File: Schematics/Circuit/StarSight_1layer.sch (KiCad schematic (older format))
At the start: 40 parts, among them IC1 LM2956-5V, J1 IR1, J10 Line1, J11 Conn_01x02, J12 Conn_01x02, J13 Conn_01x02, J14 ultSound1, J15 Conn_02x02_Counter_Clockwise, J16 ultSound1, J17 Conn_02x02_Counter_Clockwise, J18 ultSound1, J19 Conn_02x02_Counter_Clockwise, J2 Line5, J20 ultSound1, J21 Conn_01x01, J22 Conn_01x01, J23 Conn_01x01, J3 IR1, J4 Line4, J5 IR1, J6 Line3, J7 IR1, J8 Line2, J9 IR1, K1 RELAY, K2 RELAY, P1 CONN_13X2, P2 Power, Q1 Q_NMOS_GDS, Q2 Q_NMOS_GDS

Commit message: Change inductor footprint
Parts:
- L1: footprint Diodes_THT:D_5W_P5.08mm_Vertical_KathodeUp -> Inductors_THT:L_Toroid_Vertical_L16.0mm_W8.0mm_P7.62mm
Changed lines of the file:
@@
 F 0 "L1" V 3100 4500 50  0000 C CNN
 F 1 "33 uH" V 3225 4500 50  0000 C CNN
-F 2 "Diodes_THT:D_5W_P5.08mm_Vertical_KathodeUp" H 3150 4500 50  0001 C CNN
+F 2 "Inductors_THT:L_Toroid_Vertical_L16.0mm_W8.0mm_P7.62mm" H 3150 4500 50  0001 C CNN
 F 3 "" H 3150 4500 50  0001 C CNN
 	1    3150 4500

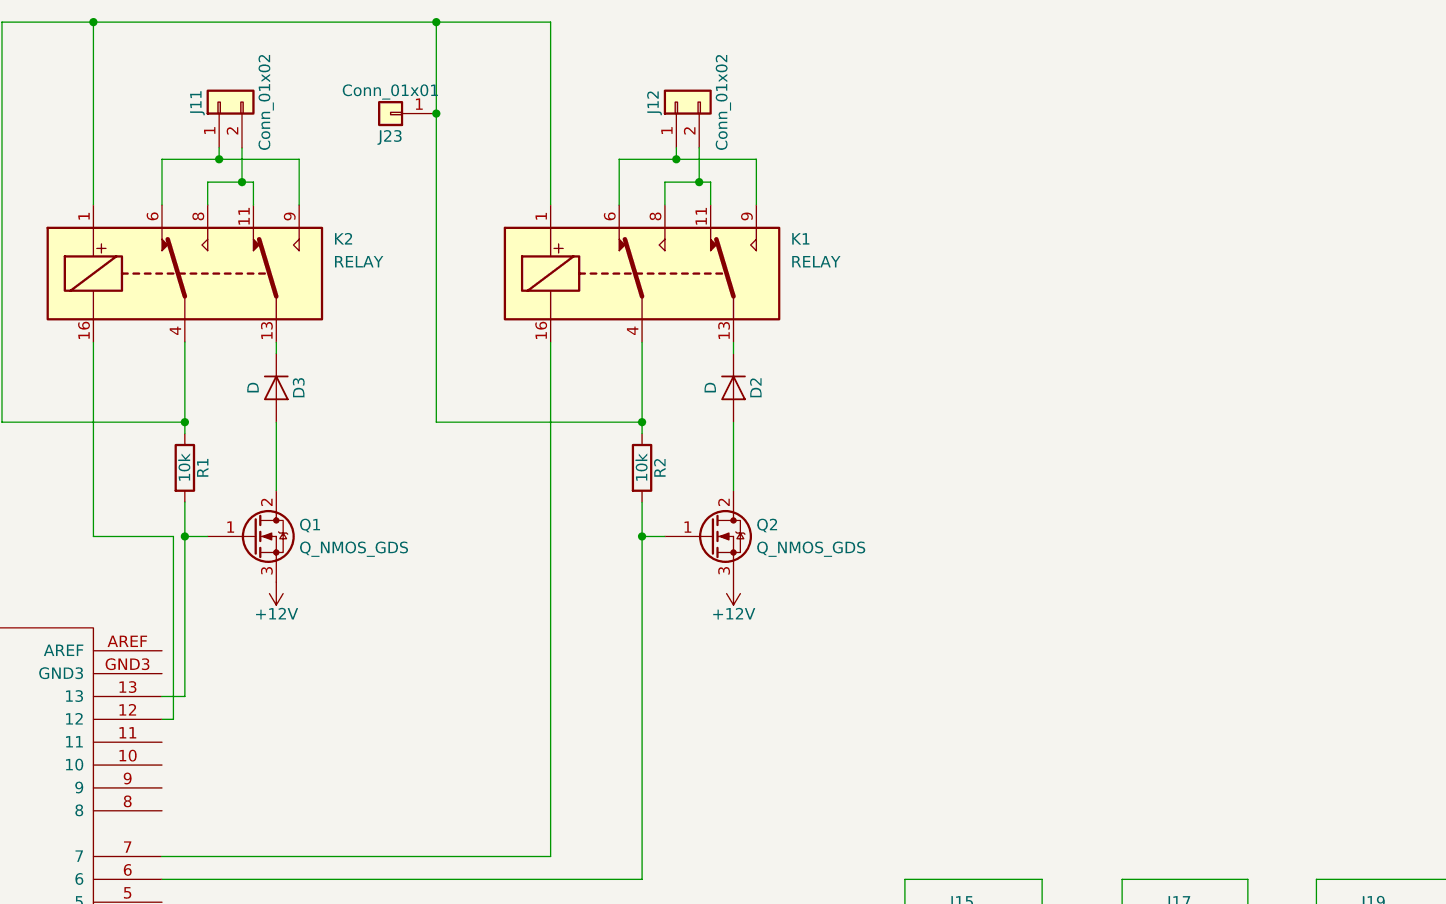
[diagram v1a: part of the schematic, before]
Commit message: Add fan
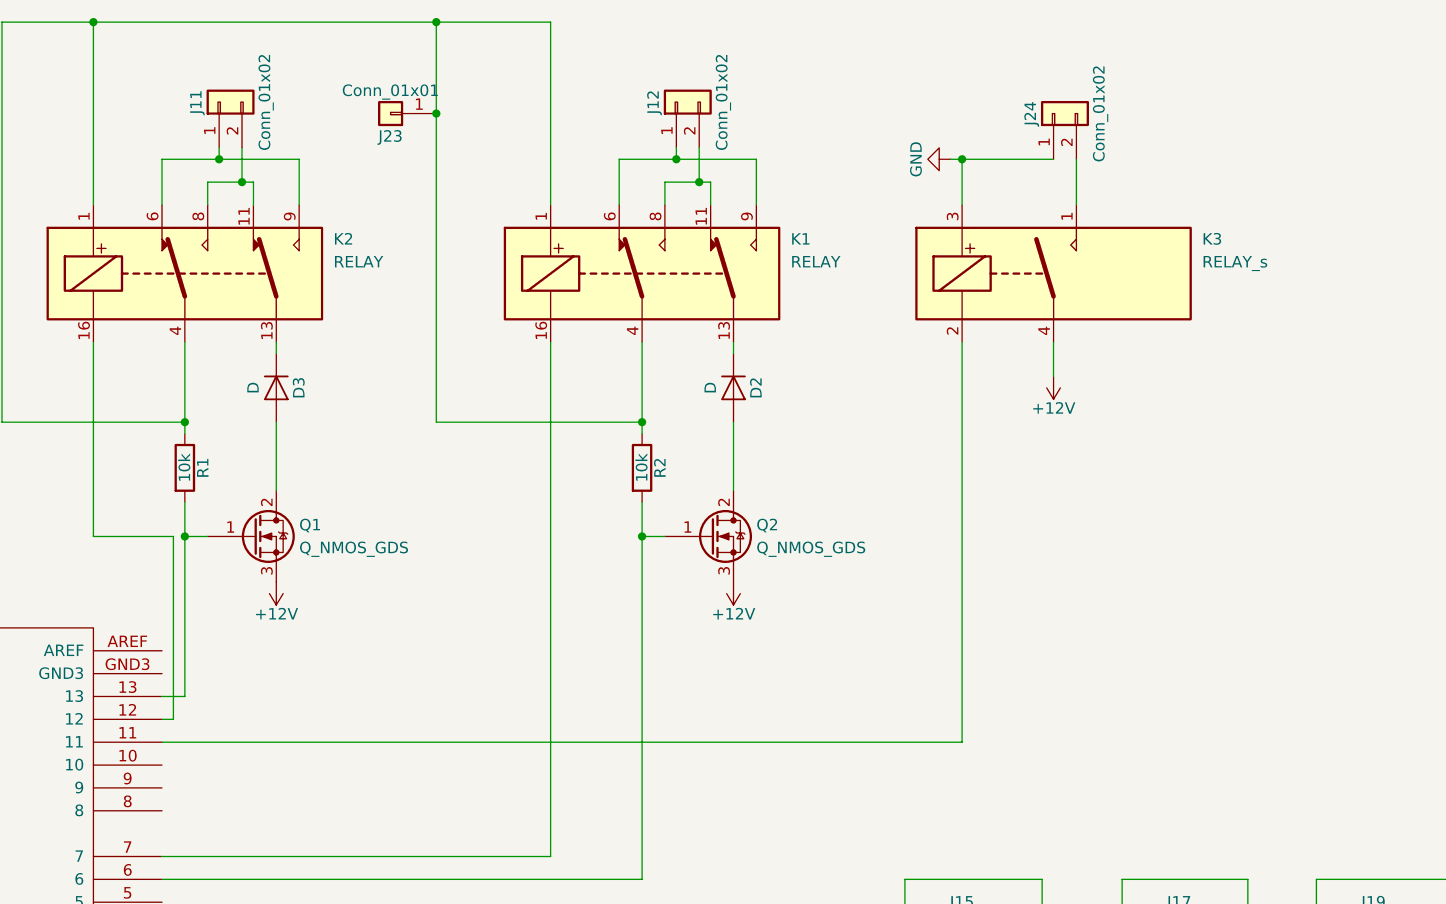
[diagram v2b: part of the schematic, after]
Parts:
- added J24: Conn_01x02, Pin_Headers:Pin_Header_Straight_1x02_Pitch2.54mm, symbol Conn_01x02
- added K3: RELAY_s, starsight:RELAY_s, symbol RELAY_s
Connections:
- net +12V: now also K3.4
- net GND: now also J24.1 (Pin_1), K3.3
- net at SHIELD1.11: now also K3.2
- new net: J24.2 (Pin_2), K3.1
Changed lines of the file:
@@
 	8950 850  11350 850
 Wire Wire Line
-	10850 2600 10850 850
+	10850 850  10850 2600
 Wire Wire Line
 	11750 4600 9650 4600
@@
 	1    0    0    -1
 $EndComp
+$Comp
+L RELAY_s K3
+U 1 1 5A820B81
+P 13350 1950
+F 0 "K3" H 14200 2100 50  0000 L CNN
+F 1 "RELAY_s" H 14200 2000 50  0000 L CNN
+F 2 "starsight:RELAY_s" H 14100 2000 50  0001 C CNN
+F 3 "" H 13350 1950 50  0001 C CNN
+	1    13350 1950
+	1    0    0    -1
+$EndComp
+Wire Wire Line
+	9650 4000 13150 4000
+Wire Wire Line
+	13150 4000 13150 2250
+$Comp
+L GND #PWR017
+U 1 1 5A821524
+P 13100 1450
+F 0 "#PWR017" H 13100 1200 50  0001 C CNN
+F 1 "GND" H 13100 1300 50  0000 C CNN
+F 2 "" H 13100 1450 50  0001 C CNN
+F 3 "" H 13100 1450 50  0001 C CNN
+	1    13100 1450
+	0    1    1    0
+$EndComp
+$Comp
+L Conn_01x02 J24
+U 1 1 5A8216F2
+P 13550 1250
+F 0 "J24" H 13550 1350 50  0000 C CNN
+F 1 "Conn_01x02" H 13550 1050 50  0000 C CNN
+F 2 "Pin_Headers:Pin_Header_Straight_1x02_Pitch2.54mm" H 13550 1250 50  0001 C CNN
+F 3 "" H 13550 1250 50  0001 C CNN
+	1    13550 1250
+	0    -1   -1   0
+$EndComp
+Wire Wire Line
+	13150 1650 13150 1450
+Wire Wire Line
+	13100 1450 13550 1450
+Connection ~ 13150 1450
+Wire Wire Line
+	13650 1650 13650 1450
+$Comp
+L +12V #PWR018
+U 1 1 5A821FE2
+P 13550 2400
+F 0 "#PWR018" H 13550 2250 50  0001 C CNN
+F 1 "+12V" H 13550 2540 50  0000 C CNN
+F 2 "" H 13550 2400 50  0001 C CNN
+F 3 "" H 13550 2400 50  0001 C CNN
+	1    13550 2400
+	-1   0    0    1
+$EndComp
+Wire Wire Line
+	13550 2250 13550 2400
 $EndSCHEMATC

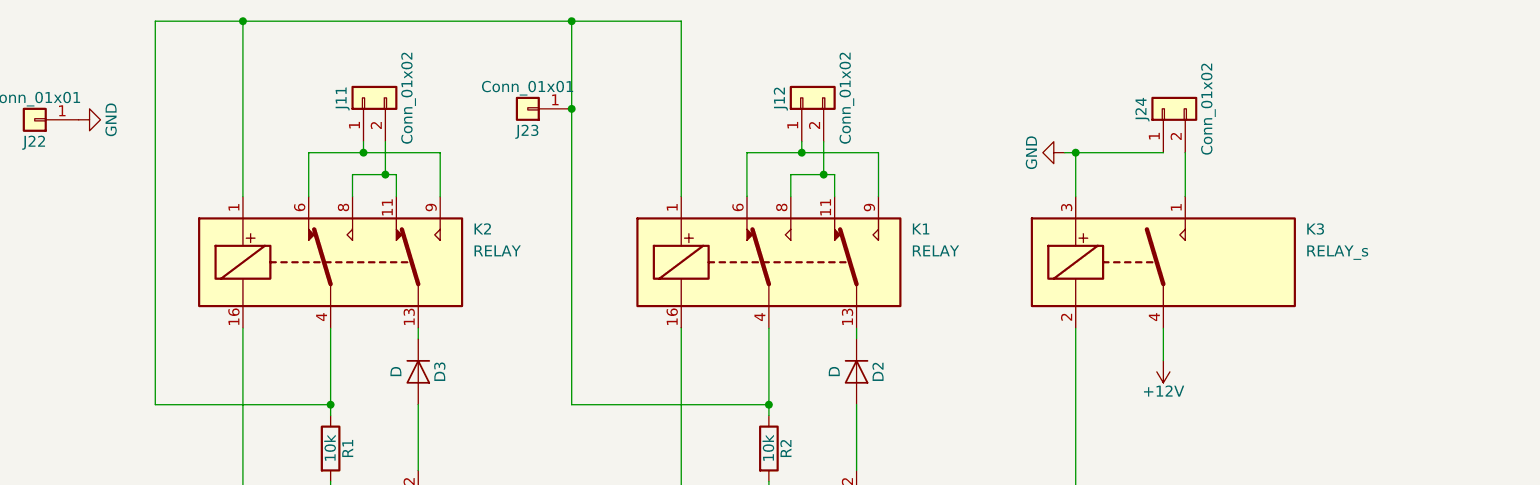
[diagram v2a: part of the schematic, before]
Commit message: Edit fan relay
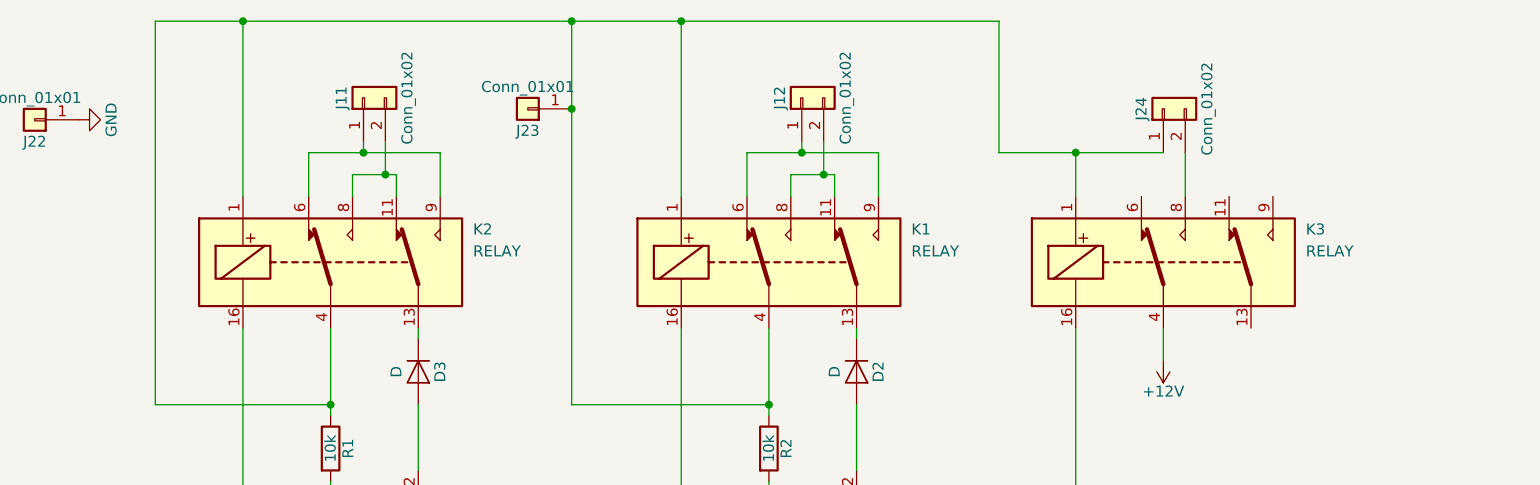
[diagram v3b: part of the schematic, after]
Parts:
- removed K3: RELAY_s, starsight:RELAY_s, symbol RELAY_s
- added K3: RELAY, Relays_THT:Relay_DPDT_Omron_G5V-2, symbol RELAY
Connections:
- net +12V: now also K3.4
- net GND: no longer J24.1 (Pin_1)
- net at SHIELD1.11: now also K3.16
- net at J23.1 (Pin_1), K1.1, K1.4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: now also J24.1 (Pin_1), K3.1
- net at J24.2 (Pin_2): now also K3.8
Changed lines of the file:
@@
 Connection ~ 10850 850
 Wire Wire Line
-	8950 850  11350 850
+	8950 850  12800 850
 Wire Wire Line
 	10850 850  10850 2600
@@
 	1    0    0    -1
 $EndComp
-$Comp
-L RELAY_s K3
-U 1 1 5A820B81
-P 13350 1950
-F 0 "K3" H 14200 2100 50  0000 L CNN
-F 1 "RELAY_s" H 14200 2000 50  0000 L CNN
-F 2 "starsight:RELAY_s" H 14100 2000 50  0001 C CNN
-F 3 "" H 13350 1950 50  0001 C CNN
-	1    13350 1950
-	1    0    0    -1
-$EndComp
 Wire Wire Line
 	9650 4000 13150 4000
 Wire Wire Line
 	13150 4000 13150 2250
-$Comp
-L GND #PWR017
-U 1 1 5A821524
-P 13100 1450
-F 0 "#PWR017" H 13100 1200 50  0001 C CNN
-F 1 "GND" H 13100 1300 50  0000 C CNN
-F 2 "" H 13100 1450 50  0001 C CNN
-F 3 "" H 13100 1450 50  0001 C CNN
-	1    13100 1450
-	0    1    1    0
-$EndComp
 $Comp
 L Conn_01x02 J24
@@
 	13150 1650 13150 1450
 Wire Wire Line
-	13100 1450 13550 1450
+	12800 1450 13550 1450
 Connection ~ 13150 1450
 Wire Wire Line
 	13650 1650 13650 1450
 $Comp
-L +12V #PWR018
+L +12V #PWR017
 U 1 1 5A821FE2
 P 13550 2400
-F 0 "#PWR018" H 13550 2250 50  0001 C CNN
+F 0 "#PWR017" H 13550 2250 50  0001 C CNN
 F 1 "+12V" H 13550 2540 50  0000 C CNN
 F 2 "" H 13550 2400 50  0001 C CNN
@@
 Wire Wire Line
 	13550 2250 13550 2400
+$Comp
+L RELAY K3
+U 1 1 5A8205E5
+P 13350 1950
+F 0 "K3" H 14200 2100 50  0000 L CNN
+F 1 "RELAY" H 14200 2000 50  0000 L CNN
+F 2 "Relays_THT:Relay_DPDT_Omron_G5V-2" H 14100 2000 50  0001 C CNN
+F 3 "" H 13350 1950 50  0001 C CNN
+	1    13350 1950
+	1    0    0    -1
+$EndComp
+Wire Wire Line
+	12800 850  12800 1450
+Connection ~ 11350 850
 $EndSCHEMATC
